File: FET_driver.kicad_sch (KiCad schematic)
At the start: 48 parts, among them Q1 TPH3R704PL,L1Q, Q10 TPH3R704PL,L1Q, Q11 TPH3R704PL,L1Q, Q12 TPH3R704PL,L1Q, Q2 TPH3R704PL,L1Q, Q3 TPH3R704PL,L1Q, Q4 TPH3R704PL,L1Q, Q5 TPH3R704PL,L1Q, Q6 TPH3R704PL,L1Q, Q7 TPH3R704PL,L1Q, Q8 TPH3R704PL,L1Q, Q9 TPH3R704PL,L1Q, U7 FD6288Q, U8 FD6288Q

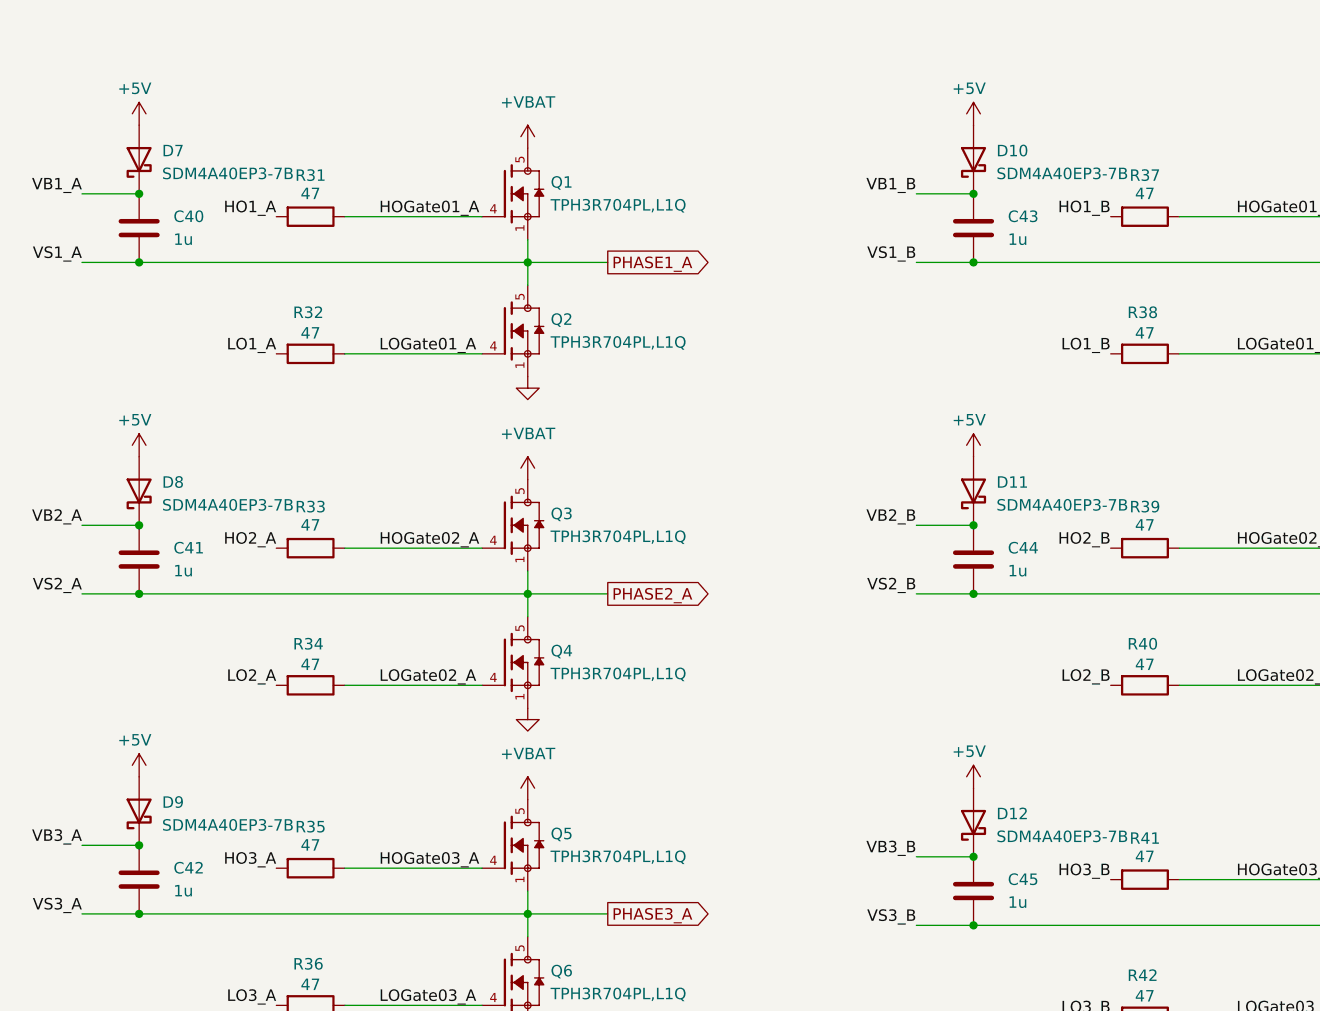
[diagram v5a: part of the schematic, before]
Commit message: change charge diodes footprint from plain 0603 to X3-TSN1608-2 which has asymetric pads
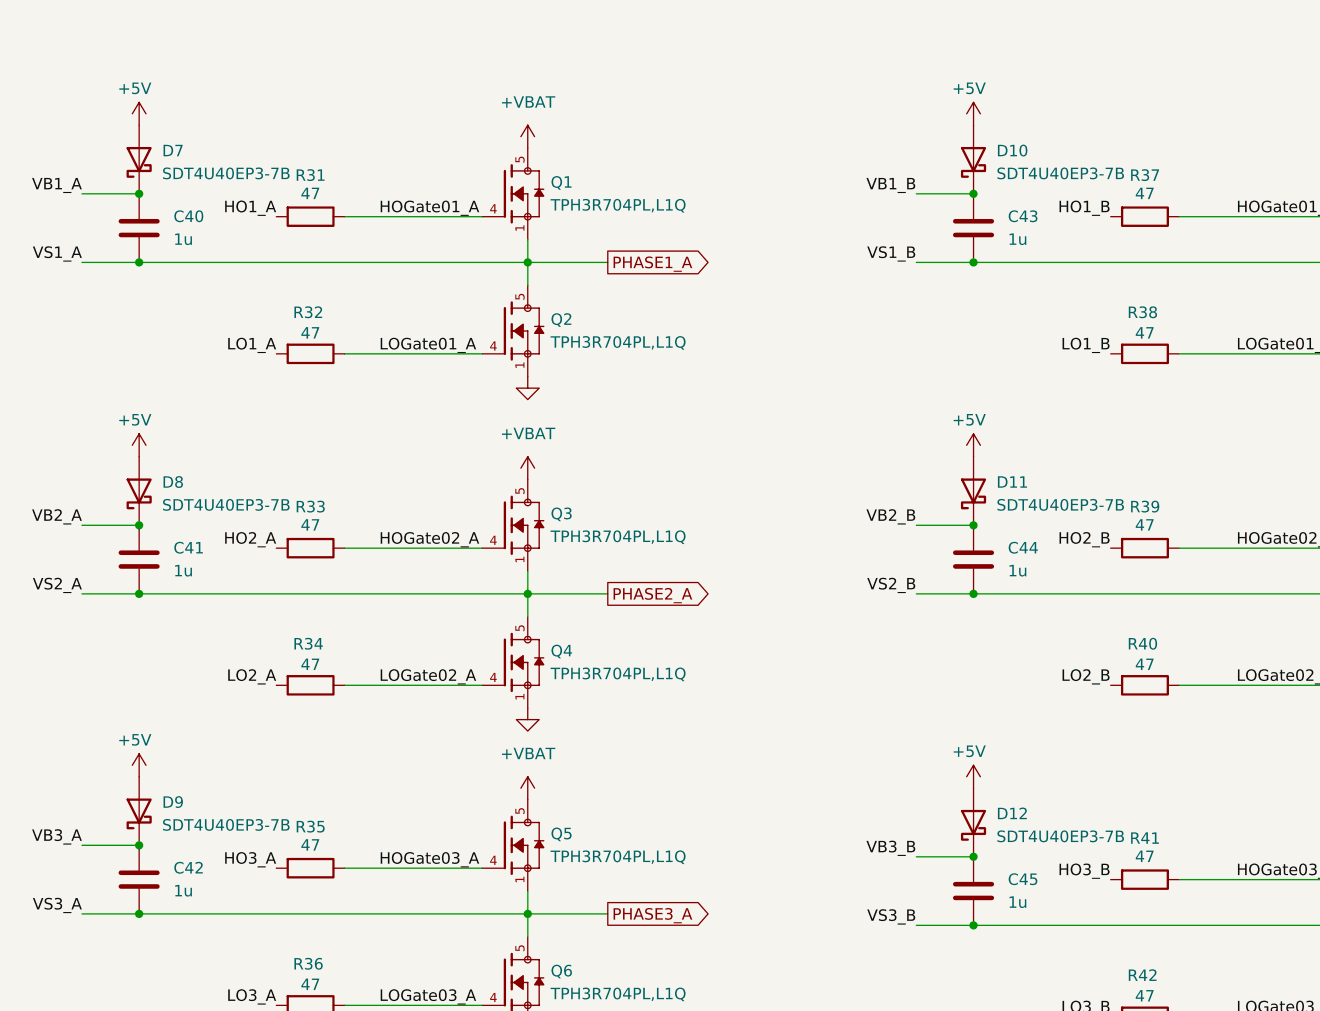
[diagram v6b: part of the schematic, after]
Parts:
- D10, D11, D12, D7, D8, D9: value SDM4A40EP3-7B -> SDT4U40EP3-7B; footprint Diode_SMD:D_0603_1608Metric -> ProjectLibrary:X3-TSN1608-2; Note SDT4U40EP3-7B -> SDM4A40EP3-7B; Part Number SDM4A40EP3-7B -> SDT4U40EP3-7B
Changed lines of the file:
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@@
 			)
 		)
-		(property "Value" "SDM4A40EP3-7B"
+		(property "Value" "SDT4U40EP3-7B "
 			(at 120.65 53.6574 90)
 			(effects
@@
 			)
 		)
-		(property "Footprint" "Diode_SMD:D_0603_1608Metric"
+		(property "Footprint" "ProjectLibrary:X3-TSN1608-2"
 			(at 118.11 52.07 0)
 			(effects
@@
 			)
 		)
-		(property "Datasheet" "https://www.diodes.com/assets/Datasheets/SDM4A40EP3.pdf"
+		(property "Datasheet" "https://www.diodes.com/assets/Datasheets/SDT4U40EP3.pdf"
 			(at 118.11 52.07 0)
 			(effects
@@
 			)
 		)
-		(property "Part Number" "SDM4A40EP3-7B"
+		(property "Part Number" "SDT4U40EP3-7B "
 			(at 118.11 52.07 0)
 			(effects
@@
 			)
 		)
-		(property "Note" "SDT4U40EP3-7B "
+		(property "Note" "SDM4A40EP3-7B"
 			(at 118.11 52.07 0)
 			(effects
@@
 			)
 		)
-		(property "Value" "SDM4A40EP3-7B"
+		(property "Value" "SDT4U40EP3-7B "
 			(at 120.65 90.4874 90)
 			(effects
@@
 			)
 		)
-		(property "Footprint" "Diode_SMD:D_0603_1608Metric"
+		(property "Footprint" "ProjectLibrary:X3-TSN1608-2"
 			(at 118.11 88.9 0)
 			(effects
@@
 			)
 		)
-		(property "Datasheet" "https://www.diodes.com/assets/Datasheets/SDM4A40EP3.pdf"
+		(property "Datasheet" "https://www.diodes.com/assets/Datasheets/SDT4U40EP3.pdf"
 			(at 118.11 88.9 0)
 			(effects
@@
 			)
 		)
-		(property "Part Number" "SDM4A40EP3-7B"
+		(property "Part Number" "SDT4U40EP3-7B "
 			(at 118.11 88.9 0)
 			(effects
@@
 			)
 		)
-		(property "Note" "SDT4U40EP3-7B "
+		(property "Note" "SDM4A40EP3-7B"
 			(at 118.11 88.9 0)
 			(effects
@@
 			)
 		)
-		(property "Value" "SDM4A40EP3-7B"
+		(property "Value" "SDT4U40EP3-7B "
 			(at 213.36 53.6574 90)
 			(effects
@@
 			)
 		)
-		(property "Footprint" "Diode_SMD:D_0603_1608Metric"
+		(property "Footprint" "ProjectLibrary:X3-TSN1608-2"
 			(at 210.82 52.07 0)
 			(effects
@@
 			)
 		)
-		(property "Datasheet" "https://www.diodes.com/assets/Datasheets/SDM4A40EP3.pdf"
+		(property "Datasheet" "https://www.diodes.com/assets/Datasheets/SDT4U40EP3.pdf"
 			(at 210.82 52.07 0)
 			(effects
@@
 			)
 		)
-		(property "Part Number" "SDM4A40EP3-7B"
+		(property "Part Number" "SDT4U40EP3-7B "
 			(at 210.82 52.07 0)
 			(effects
@@
 			)
 		)
-		(property "Note" "SDT4U40EP3-7B "
+		(property "Note" "SDM4A40EP3-7B"
 			(at 210.82 52.07 0)
 			(effects
@@
 			)
 		)
-		(property "Value" "SDM4A40EP3-7B"
+		(property "Value" "SDT4U40EP3-7B "
 			(at 213.36 127.3174 90)
 			(effects
@@
 			)
 		)
-		(property "Footprint" "Diode_SMD:D_0603_1608Metric"
+		(property "Footprint" "ProjectLibrary:X3-TSN1608-2"
 			(at 210.82 125.73 0)
 			(effects
@@
 			)
 		)
-		(property "Datasheet" "https://www.diodes.com/assets/Datasheets/SDM4A40EP3.pdf"
+		(property "Datasheet" "https://www.diodes.com/assets/Datasheets/SDT4U40EP3.pdf"
 			(at 210.82 125.73 0)
 			(effects
@@
 			)
 		)
-		(property "Part Number" "SDM4A40EP3-7B"
+		(property "Part Number" "SDT4U40EP3-7B "
 			(at 210.82 125.73 0)
 			(effects
@@
 			)
 		)
-		(property "Note" "SDT4U40EP3-7B "
+		(property "Note" "SDM4A40EP3-7B"
 			(at 210.82 125.73 0)
 			(effects
@@
 			)
 		)
-		(property "Value" "SDM4A40EP3-7B"
+		(property "Value" "SDT4U40EP3-7B "
 			(at 120.65 126.0474 90)
 			(effects
@@
 			)
 		)
-		(property "Footprint" "Diode_SMD:D_0603_1608Metric"
+		(property "Footprint" "ProjectLibrary:X3-TSN1608-2"
 			(at 118.11 124.46 0)
 			(effects
@@
 			)
 		)
-		(property "Datasheet" "https://www.diodes.com/assets/Datasheets/SDM4A40EP3.pdf"
+		(property "Datasheet" "https://www.diodes.com/assets/Datasheets/SDT4U40EP3.pdf"
 			(at 118.11 124.46 0)
 			(effects
@@
 			)
 		)
-		(property "Part Number" "SDM4A40EP3-7B"
+		(property "Part Number" "SDT4U40EP3-7B "
 			(at 118.11 124.46 0)
 			(effects
@@
 			)
 		)
-		(property "Note" "SDT4U40EP3-7B "
+		(property "Note" "SDM4A40EP3-7B"
 			(at 118.11 124.46 0)
 			(effects
@@
 			)
 		)
-		(property "Value" "SDM4A40EP3-7B"
+		(property "Value" "SDT4U40EP3-7B "
 			(at 213.36 90.4874 90)
 			(effects
@@
 			)
 		)
-		(property "Footprint" "Diode_SMD:D_0603_1608Metric"
+		(property "Footprint" "ProjectLibrary:X3-TSN1608-2"
 			(at 210.82 88.9 0)
 			(effects
@@
 			)
 		)
-		(property "Datasheet" "https://www.diodes.com/assets/Datasheets/SDM4A40EP3.pdf"
+		(property "Datasheet" "https://www.diodes.com/assets/Datasheets/SDT4U40EP3.pdf"
 			(at 210.82 88.9 0)
 			(effects
@@
 			)
 		)
-		(property "Part Number" "SDM4A40EP3-7B"
+		(property "Part Number" "SDT4U40EP3-7B "
 			(at 210.82 88.9 0)
 			(effects
@@
 			)
 		)
-		(property "Note" "SDT4U40EP3-7B "
+		(property "Note" "SDM4A40EP3-7B"
 			(at 210.82 88.9 0)
 			(effects
